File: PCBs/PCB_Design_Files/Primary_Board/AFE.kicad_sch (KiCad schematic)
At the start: 0 parts

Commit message: AFE schematic, added 0603 component libraries
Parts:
- added C1, C3: 1u, Project Footprints:0603_capacitor, symbol project_symbols:0603_capacitor
- added C2: 2.2p, Project Footprints:0603_capacitor, symbol project_symbols:0603_capacitor
- added C4, C8, C9: .1u, Project Footprints:0603_capacitor, symbol project_symbols:0603_capacitor
- added C5: 3.9u, Project Footprints:0603_capacitor, symbol project_symbols:0603_capacitor
- added C6, C7: 220n, Project Footprints:0603_capacitor, symbol project_symbols:0603_capacitor
- added LED1: SFH 2704, Project Footprints:SFH2704_LED, symbol project_symbols:SFH_2704
- added R1, R3: 100k, Project Footprints:0603_resistor, symbol project_symbols:0603_resistor
- added R10: 41.2k, Project Footprints:0603_resistor, symbol project_symbols:0603_resistor
- added R11, R8, R9: 10k, Project Footprints:0603_resistor, symbol project_symbols:0603_resistor
- added R2: 150k, Project Footprints:0603_resistor, symbol project_symbols:0603_resistor
- added R4, R5: 120k, Project Footprints:0603_resistor, symbol project_symbols:0603_resistor
- added R6: 1k, Project Footprints:0603_resistor, symbol project_symbols:0603_resistor
- added R7: 380k, Project Footprints:0603_resistor, symbol project_symbols:0603_resistor
- added U1: OPA381, Project Footprints:OPA381, symbol project_symbols:OPA381
- added U2, U3, U4: TLV9002, Project Footprints:TLV9002, symbol project_symbols:TLV9002
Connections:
- new net: C5.2, R3.1, R4.1
- new net: C6.1, R4.2, R5.1
- new net: C2.1, LED1.1, R2.1, U1.2 (IN-)
- new net: C1.1, R1.1, U1.3 (IN+)
- new net: R8.2, R9.1, U4.3 (IN1+)
- new net: C6.2, U2.1 (OUT1), U2.2 (IN1-), U2.5 (IN2+)
- new net: C7.1, R5.2, U2.3 (IN1+)
- new net: R6.1, R7.1, U2.6 (IN2-)
- new net: R10.2, R11.1, U4.5 (IN2+)
- new net: U3.6 (IN2-), U3.7 (OUT2)
- new net +1.65V: C7.2, R3.2, R6.2, U4.1 (OUT1), U4.2 (IN1-)
- new net +3V3: C3.1, C4.1, C8.1, C9.1, R8.1, U1.7 (V+), U2.8 (V+), U3.8 (V+), U4.8 (V+)
- new net ADC_AC: R7.2, U2.7 (OUT2)
- new net ADC_DC: U3.1 (OUT1), U3.2 (IN1-)
- new net GND: C1.2, C3.2, C4.2, C8.2, C9.2, LED1.2, R11.2, R9.2, U1.4 (V-), U2.4 (V-), U3.4 (V-), U3.5 (IN2+), U4.4 (V-)
- new net TIA_Out: C2.2, C5.1, R2.2, U1.6 (OUTPUT), U3.3 (IN1+)
- new net V_bandgap: R10.1
- new net Vref: R1.2, U4.6 (IN2-), U4.7 (OUT2)
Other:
- note added: "0.6Hz HPF"
- note added: "6Hz Active LPF Non-Inverting Amplifier (380 Gain)"
- note added: "Analog Front End"
- note added: "DC Buffer"
- note added: "Local Voltage References (+1.65V, +0.3V)"
- note added: "Photodiode"
- note added: "TIA (150k Gain)"
- note added: "TIA_Out = Vref + (Ipd*150k)"
- note added: "Unused Opamp"

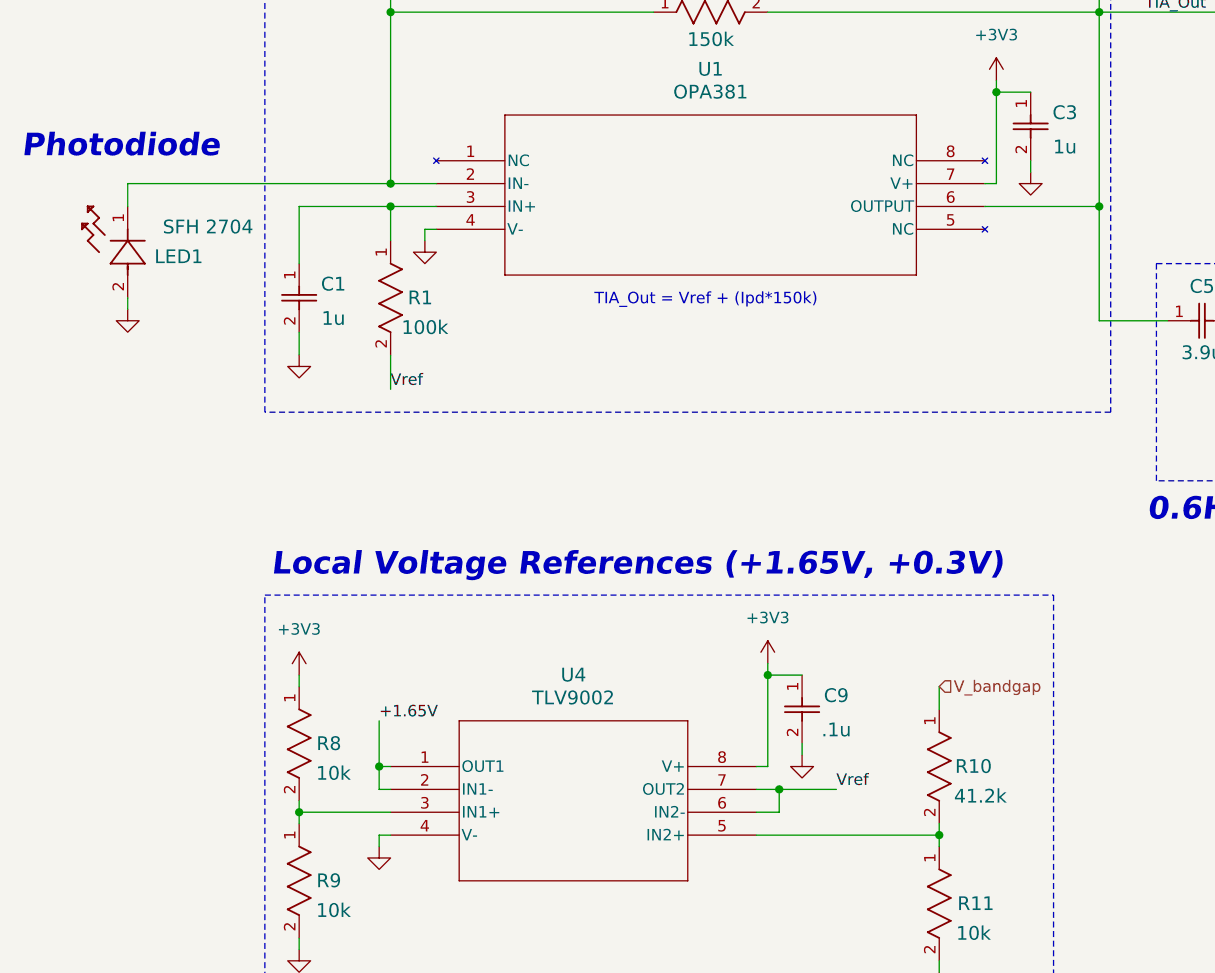
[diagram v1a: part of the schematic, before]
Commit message: ptat_bandgap component libraries
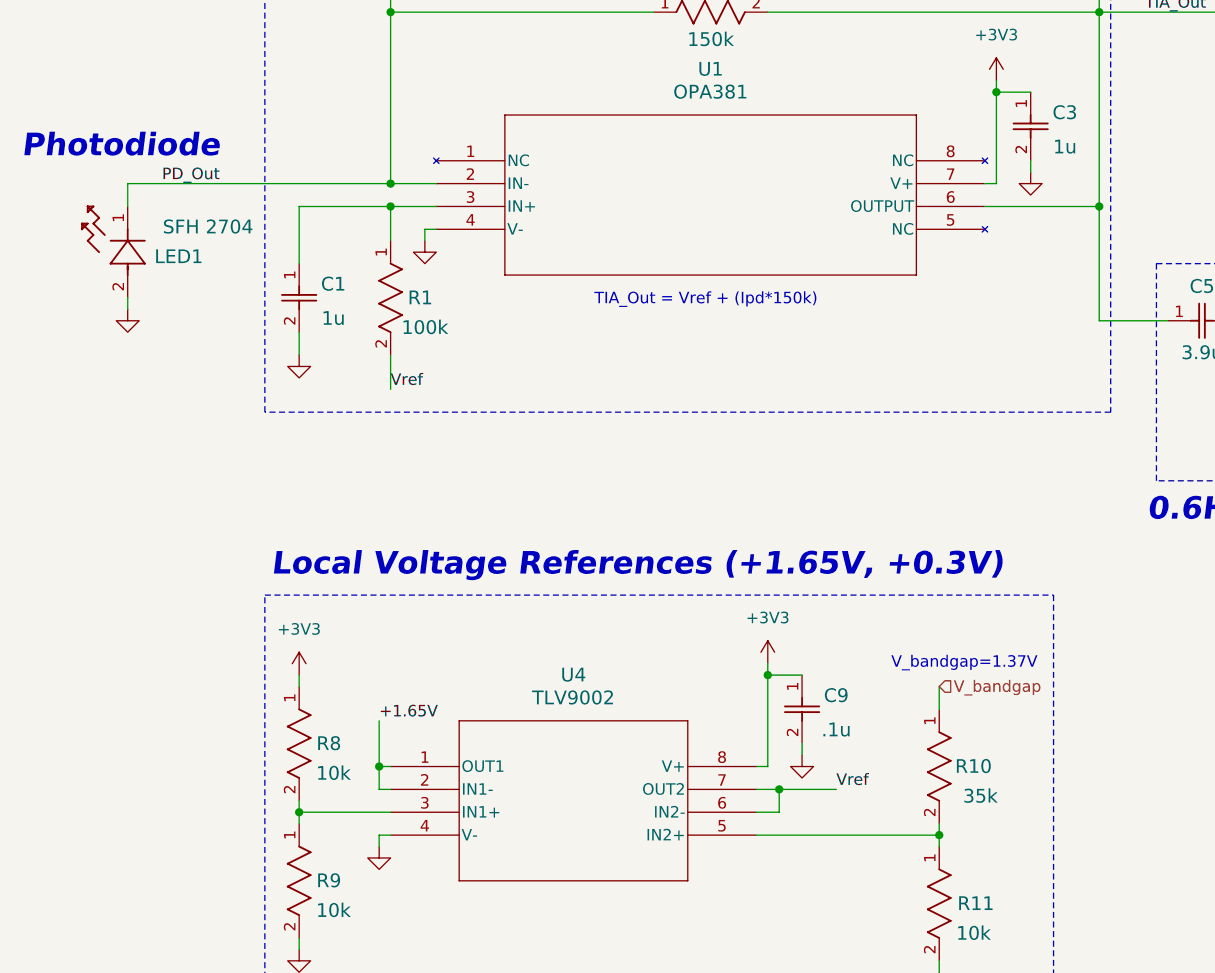
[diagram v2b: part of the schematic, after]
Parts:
- R10: value 41.2k -> 35k
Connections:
- net PD_Out: now reaches C2.1, LED1.1, R2.1, U1.2 (IN-)
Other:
- note added: "V_bandgap=1.37V"
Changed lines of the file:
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@@
+		)
+	)
+	(text "V_bandgap=1.37V"
+		(exclude_from_sim no)
+		(at 119.634 128.27 0)
+		(effects
+			(font
+				(size 1.27 1.27)
+			)
 		)
 	)
@@
 	(label "+1.65V"
 		(at 251.46 106.68 0)
+		(effects
+			(font
+				(size 1.27 1.27)
+			)
+			(justify left bottom)
+		)
+	)
+	(label "PD_Out"
+		(at 30.48 74.93 0)
 		(effects
 			(font
@@
 			)
 		)
-		(property "Value" "41.2k"
+		(property "Value" "35k"
 			(at 121.412 143.002 90)
 			(effects

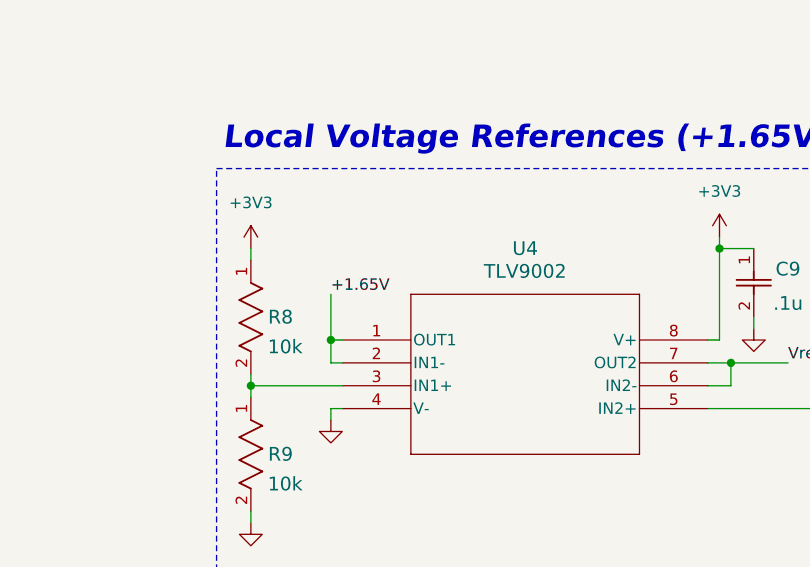
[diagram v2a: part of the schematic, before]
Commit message: added some parts of schematic
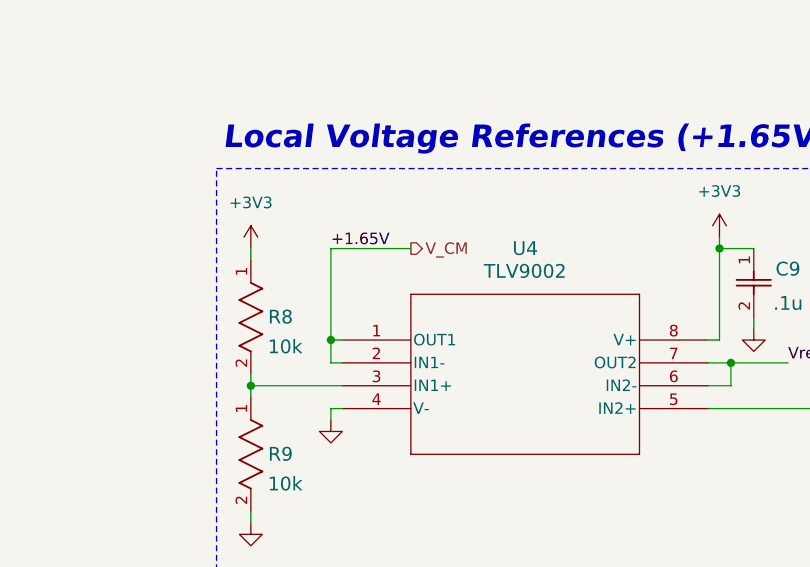
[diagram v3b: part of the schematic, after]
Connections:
- net +1.65V renamed V_CM
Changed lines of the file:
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@@
 	(wire
 		(pts
-			(xy 54.61 134.62) (xy 54.61 139.7)
+			(xy 54.61 129.54) (xy 54.61 139.7)
 		)
 		(stroke
@@
 		(pts
 			(xy 257.81 87.63) (xy 257.81 85.09)
+		)
+		(stroke
+			(width 0)
+			(type default)
+		)
+	)
+	(wire
+		(pts
+			(xy 54.61 129.54) (xy 63.5 129.54)
 		)
 		(stroke
@@
 	)
 	(label "+1.65V"
-		(at 54.61 134.62 0)
+		(at 54.61 129.54 0)
 		(effects
 			(font
@@
 		(effects
 			(font
+				(size 1.27 1.27)
+			)
+			(justify left)
+		)
+	)
+	(hierarchical_label "V_CM"
+		(shape output)
+		(at 63.5 129.54 0)
+		(effects
+			(font

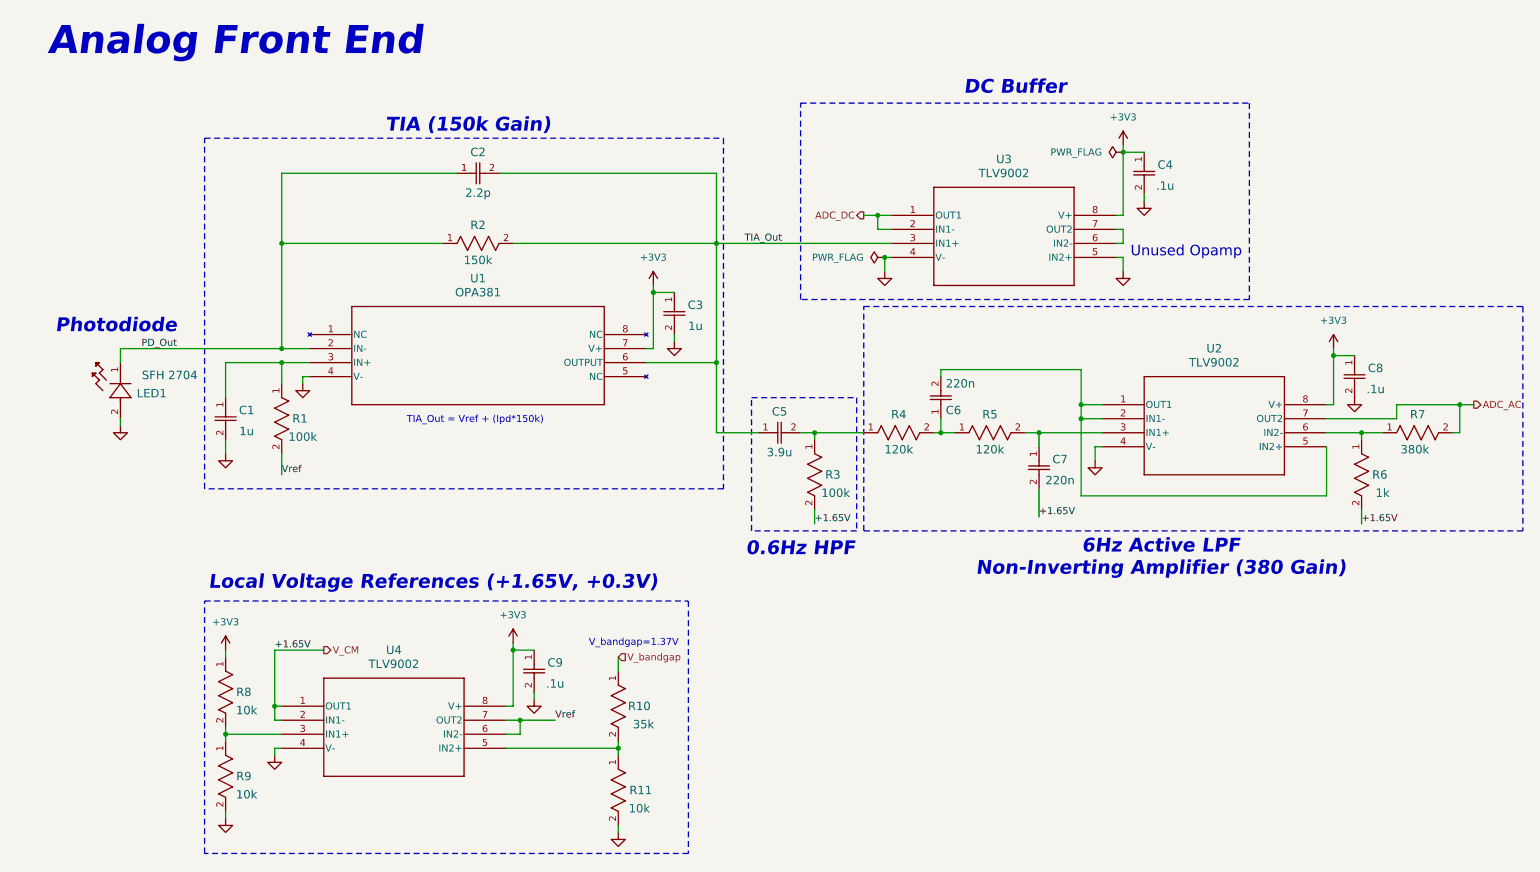
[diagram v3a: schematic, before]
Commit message: added 3rd order filter
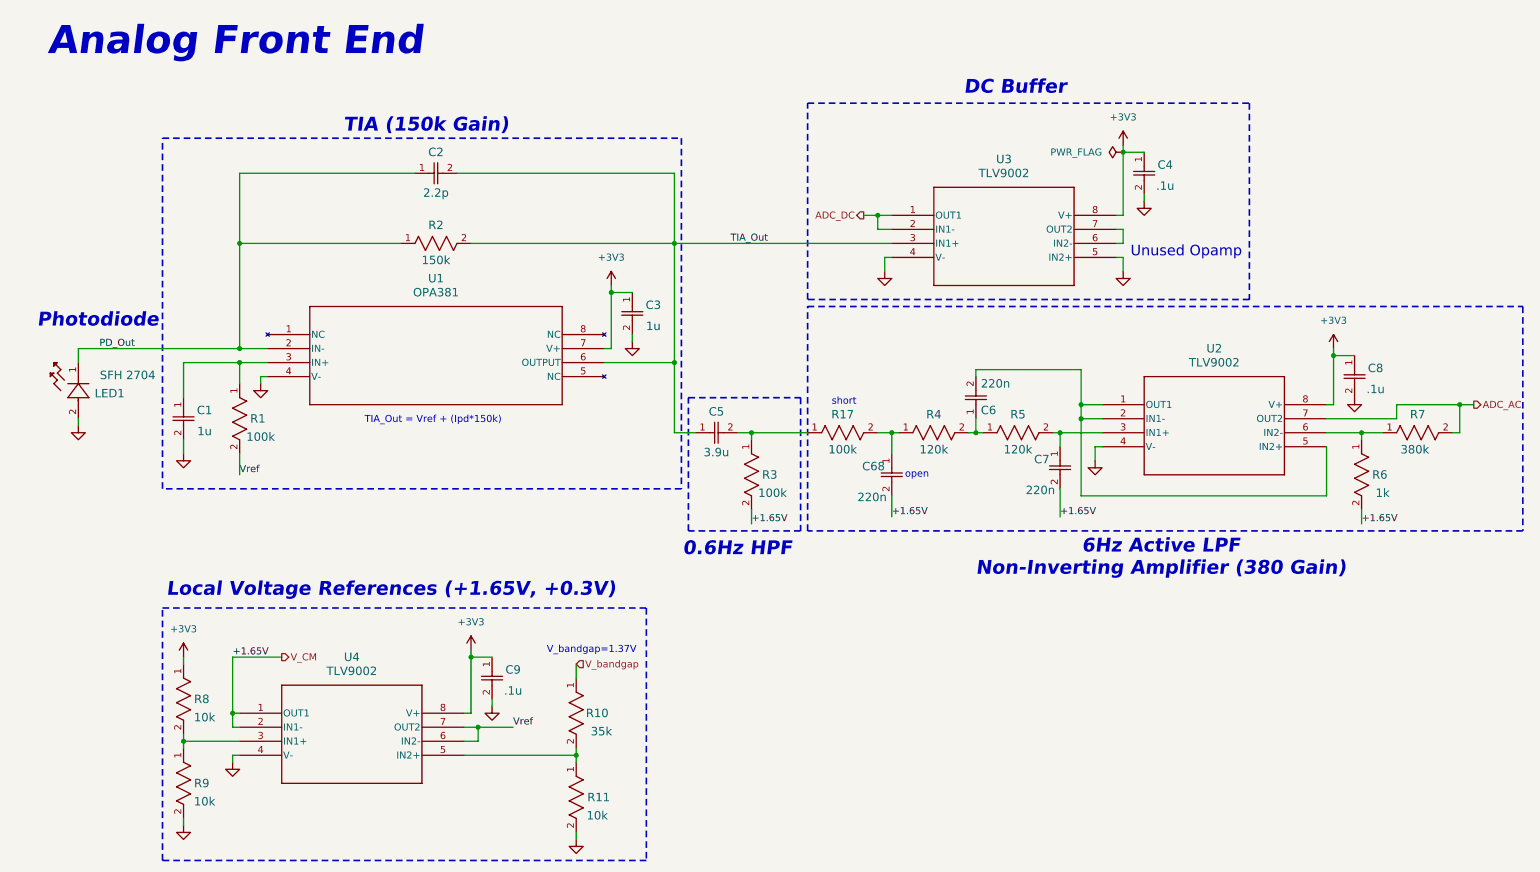
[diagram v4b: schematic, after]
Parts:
- added C68: 220n, Project Footprints:0603_capacitor, symbol project_symbols:0603_capacitor
- added R17: 100k, Project Footprints:0603_resistor, symbol project_symbols:0603_resistor
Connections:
- net V_CM: now also C68.2
- net at C5.2, R3.1: now also R17.1; no longer R4.1
- new net: C68.1, R17.2, R4.1
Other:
- note added: "open"
- note added: "short"
- moved on the sheet: C1, C2, C3, C5, C6, C7, C9, LED1, R1, R10, R11, R2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

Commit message: added bypass
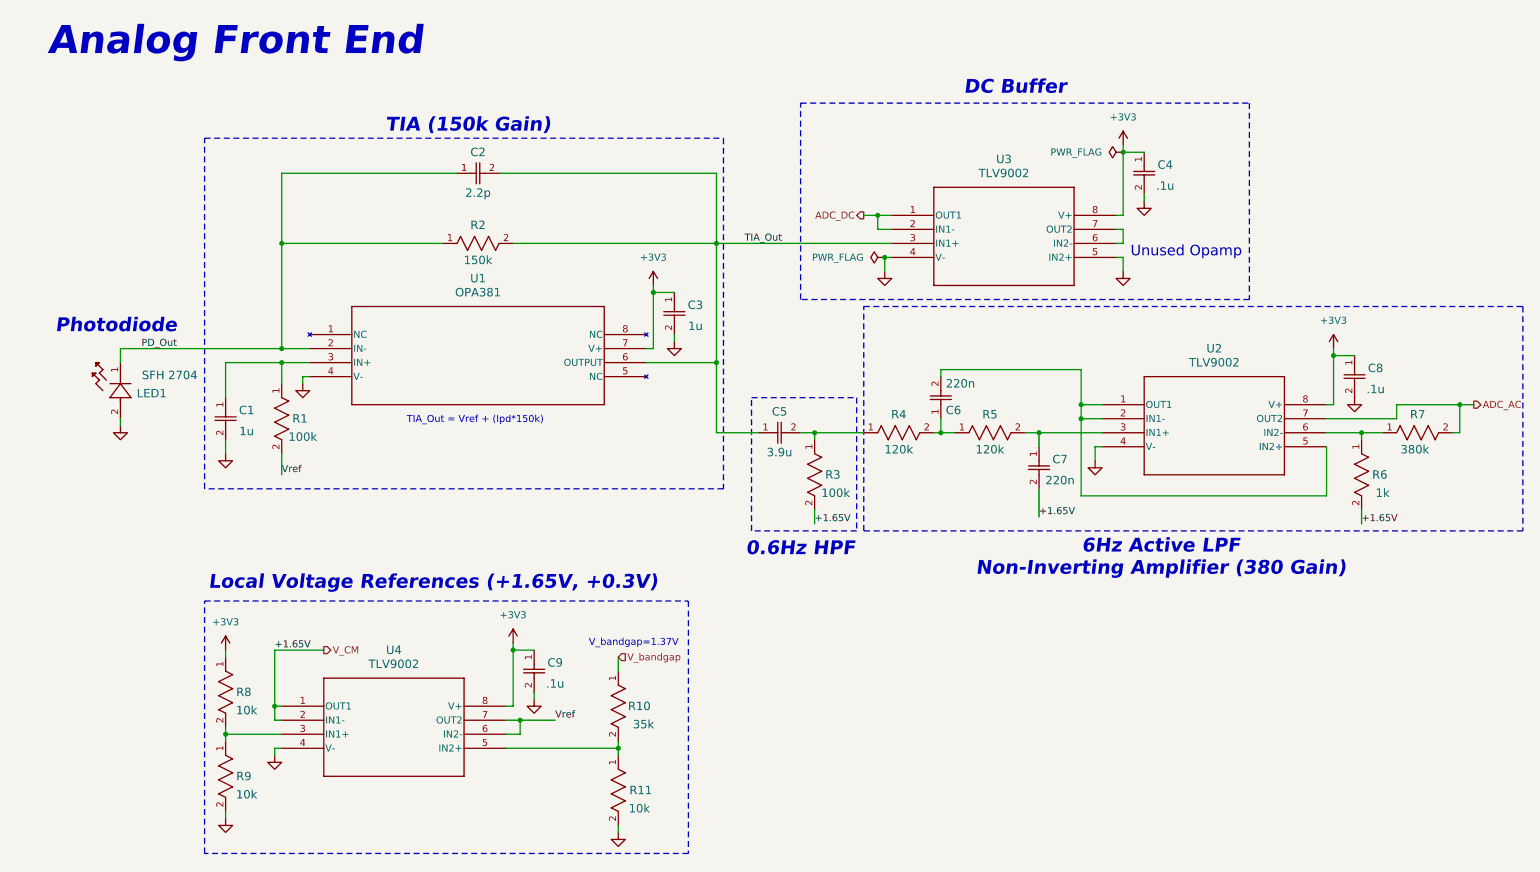
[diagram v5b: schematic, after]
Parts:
- removed C68: 220n, Project Footprints:0603_capacitor, symbol project_symbols:0603_capacitor
- removed R17: 100k, Project Footprints:0603_resistor, symbol project_symbols:0603_resistor
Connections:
- net at R4.1: now also C5.2, R3.1
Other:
- note removed: "open"
- note removed: "short"
- moved on the sheet: C1, C2, C3, C5, C6, C7, C9, LED1, R1, R10, R11, R2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

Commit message: updated AFE pcb
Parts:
- removed C4: .1u, Project Footprints:0603_capacitor, symbol project_symbols:0603_capacitor
- removed U3: TLV9002, Project Footprints:TLV9002, symbol project_symbols:TLV9002
- added C68: 220n, Project Footprints:0603_capacitor, symbol project_symbols:0603_capacitor
- added R17: 100k, Project Footprints:0603_resistor, symbol project_symbols:0603_resistor
- R10: value 35k -> 40k
- R4, R5: value 120k -> 100k
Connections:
- net TIA_Out is gone; now on net ADC_DC: C2.2, C5.1, R2.2, U1.6 (OUTPUT)
- net V_CM: now also C68.2
- net at C5.2, R3.1: now also R17.1; no longer R4.1
- new net: C68.1, R17.2, R4.1
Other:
- note added: "7Hz Active LPF Non-Inverting Amplifier (380 Gain)"
- note added: "V_bandgap=1.25V"
- note removed: "6Hz Active LPF Non-Inverting Amplifier (380 Gain)"
- note removed: "DC Buffer"
- note removed: "Unused Opamp"
- note removed: "V_bandgap=1.37V"
- moved on the sheet: C1, C2, C3, C5, C6, C7, C8, C9, LED1, R1, R10, R11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

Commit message: TH header labels
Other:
- note added: "fc = 1/(2pi(100k)(220n)) ~= 7Hz Av = (1+380k/1k) ~= 380"
- note added: "open"
- note added: "short"
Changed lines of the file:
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@@
+		)
+	)
+	(text "short\n"
+		(exclude_from_sim no)
+		(at 63.5 145.288 0)
+		(effects
+			(font
+				(size 1.27 1.27)
+			)
 		)
 	)
@@
 			)
 		)
+	)
+	(text "open\n"
+		(exclude_from_sim no)
+		(at 69.342 148.844 0)
+		(effects
+			(font
+				(size 1.27 1.27)
+			)
+		)
+	)
+	(text "fc = 1/(2pi(100k)(220n)) ~= 7Hz\n\nAv = (1+380k/1k) ~= 380"
+		(exclude_from_sim no)
+		(at 71.374 121.666 0)
+		(effects
+			(font
+				(size 1.27 1.27)
+			)
+		)
